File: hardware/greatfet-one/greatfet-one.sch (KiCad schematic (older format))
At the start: 99 parts, among them J1 NEIGHBOR1, J2 NEIGHBOR2, J3 USB-MICRO-B-SHIELDED, J4 USB-MICRO-B-SHIELDED, J5 JTAG, J6 POWER, J7 BONUS_ROW, SW1 DFU, SW2 RESET, U1 LPC4330FBD144, U2 W25Q16DV, U3 AP7333, U4 IP4220CZ6, U5 AP2553W6-7, X1 MCU_XTAL, X2 RTC_XTAL

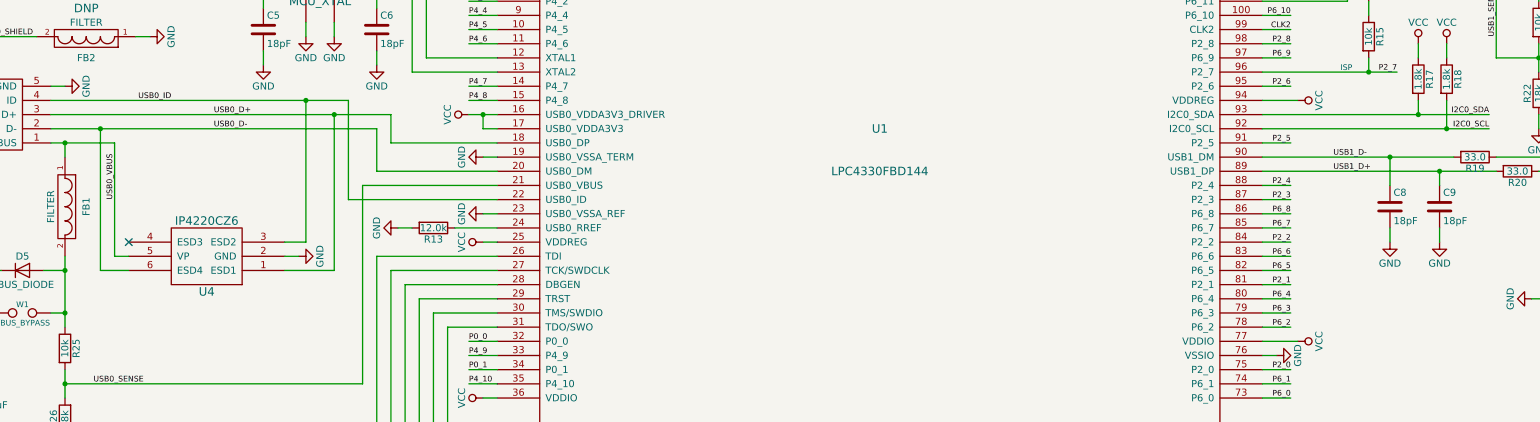
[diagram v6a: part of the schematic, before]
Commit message: GreatFET One: added 15k pull-down resistors to USB signals to support host mode
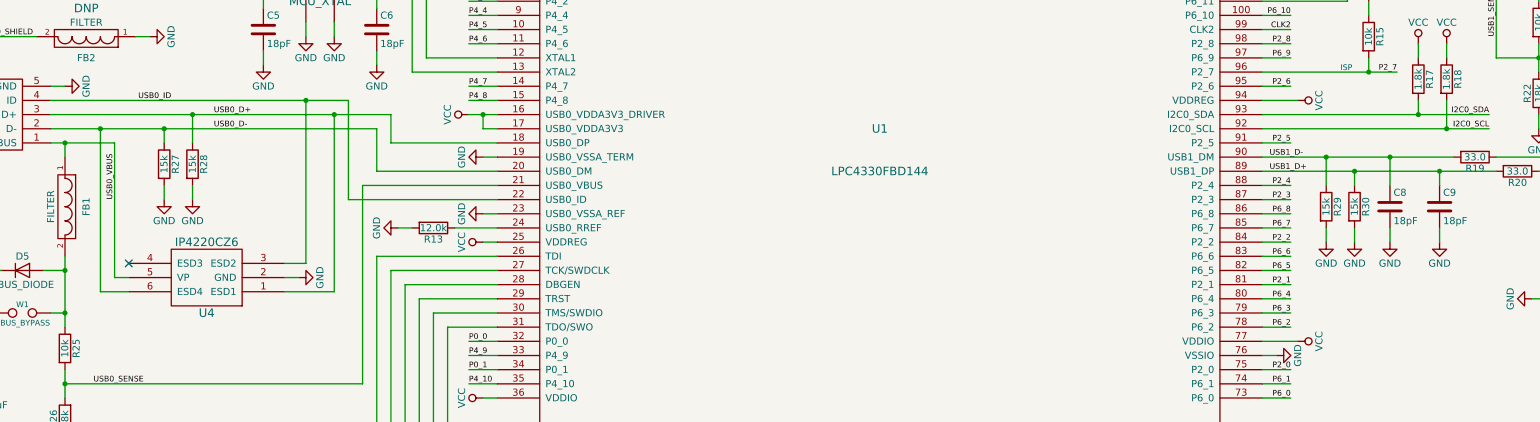
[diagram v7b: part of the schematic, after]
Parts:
- added R27, R28, R29, R30: 15k, gsg-modules:0603, symbol R
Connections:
- net GND: now also R27.2, R28.2, R29.2, R30.2
- net USB0_D+: now also R28.1
- net USB0_D-: now also R27.1
- net USB1_D+: now also R30.1
- net USB1_D-: now also R29.1
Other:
- moved on the sheet: U4
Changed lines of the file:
@@
 EESchema Schematic File Version 2
-LIBS:greatfet-one-rescue
 LIBS:power
 LIBS:device
@@
 LIBS:contrib
 LIBS:valves
-LIBS:gsg-symbols
 LIBS:greatfet-one-cache
 EELAYER 25 0
@@
 L IP4220CZ6 U4
 U 1 1 55E0B467
-P 3800 6100
-F 0 "U4" H 3800 6350 60  0000 C CNN
-F 1 "IP4220CZ6" H 3800 5850 60  0000 C CNN
-F 2 "gsg-modules:SOT457" H 3800 6100 60  0001 C CNN
-F 3 "" H 3800 6100 60  0000 C CNN
-F 4 "NXP" H 3800 6100 60  0001 C CNN "Manufacturer"
-F 5 "IP4220CZ6,125" H 3800 6100 60  0001 C CNN "Part Number"
-F 6 "IC USB DUAL ESD PROTECT 6TSOP" H 3800 6100 60  0001 C CNN "Description"
-	1    3800 6100
+P 3800 6250
+F 0 "U4" H 3800 6500 60  0000 C CNN
+F 1 "IP4220CZ6" H 3800 6000 60  0000 C CNN
+F 2 "gsg-modules:SOT457" H 3800 6250 60  0001 C CNN
+F 3 "" H 3800 6250 60  0000 C CNN
+F 4 "NXP" H 3800 6250 60  0001 C CNN "Manufacturer"
+F 5 "IP4220CZ6,125" H 3800 6250 60  0001 C CNN "Part Number"
+F 6 "IC USB DUAL ESD PROTECT 6TSOP" H 3800 6250 60  0001 C CNN "Description"
+	1    3800 6250
 	-1   0    0    1
 $EndComp
@@
 L GND #PWR011
 U 1 1 55E3AB7C
-P 4450 6100
-F 0 "#PWR011" H 4450 5850 50  0001 C CNN
-F 1 "GND" H 4450 5950 50  0000 C CNN
-F 2 "" H 4450 6100 60  0000 C CNN
-F 3 "" H 4450 6100 60  0000 C CNN
-	1    4450 6100
+P 4450 6250
+F 0 "#PWR011" H 4450 6000 50  0001 C CNN
+F 1 "GND" H 4450 6100 50  0000 C CNN
+F 2 "" H 4450 6250 60  0000 C CNN
+F 3 "" H 4450 6250 60  0000 C CNN
+	1    4450 6250
 	0    -1   -1   0
 $EndComp
@@
 Text Label 3850 5200 0    40   ~ 0
 USB0_D-
-Text Label 11750 5400 0    40   ~ 0
+Text Label 11300 5400 0    40   ~ 0
 USB1_D-
-Text Label 11750 5500 0    40   ~ 0
+Text Label 11300 5500 0    40   ~ 0
 USB1_D+
-NoConn ~ 3250 6000
+NoConn ~ 3250 6150
 Text Label 2200 4550 0    40   ~ 0
 USB0_SHIELD
@@
 	0    1    1    0
 $EndComp
+$Comp
+L VCC #PWR092
+U 1 1 57C6226E
+P 5900 1400
+F 0 "#PWR092" H 5900 1250 50  0001 C CNN
+F 1 "VCC" H 5900 1550 50  0000 C CNN
+F 2 "" H 5900 1400 60  0000 C CNN
+F 3 "" H 5900 1400 60  0000 C CNN
+	1    5900 1400
+	0    -1   -1   0
+$EndComp
+Text Label 5750 1200 0    40   ~ 0
+USB1_VBUS
+$Comp
+L TEST_2P W1
+U 1 1 57C655EF
+P 2500 6500
+F 0 "W1" H 2500 6560 40  0000 C CNN
+F 1 "VBUS_BYPASS" H 2500 6430 40  0000 C CNN
+F 2 "gsg-modules:0603-JUMPER" H 2500 6500 60  0001 C CNN
+F 3 "" H 2500 6500 60  0000 C CNN
+	1    2500 6500
+	1    0    0    -1
+$EndComp
+$Comp
+L R R28
+U 1 1 5A48D952
+P 3700 5450
+F 0 "R28" V 3780 5450 50  0000 C CNN
+F 1 "15k" V 3700 5450 50  0000 C CNN
+F 2 "gsg-modules:0603" V 3630 5450 30  0001 C CNN
+F 3 "" H 3700 5450 30  0000 C CNN
+F 4 "Yageo" H 3700 5450 60  0001 C CNN "Manufacturer"
+F 5 "RC0603JR-0715KL" H 3700 5450 60  0001 C CNN "Part Number"
+F 6 "RES SMD 15K OHM 5% 1/10W 0603" H 3700 5450 60  0001 C CNN "Description"
+	1    3700 5450
+	1    0    0    -1
+$EndComp
+$Comp
+L R R27
+U 1 1 5A48E55C
+P 3500 5450
+F 0 "R27" V 3580 5450 50  0000 C CNN
+F 1 "15k" V 3500 5450 50  0000 C CNN
+F 2 "gsg-modules:0603" V 3430 5450 30  0001 C CNN
+F 3 "" H 3500 5450 30  0000 C CNN
+F 4 "Yageo" H 3500 5450 60  0001 C CNN "Manufacturer"
+F 5 "RC0603JR-0715KL" H 3500 5450 60  0001 C CNN "Part Number"
+F 6 "RES SMD 15K OHM 5% 1/10W 0603" H 3500 5450 60  0001 C CNN "Description"
+	1    3500 5450
+	1    0    0    -1
+$EndComp
+$Comp
+L GND #PWR093
+U 1 1 5A48EE95
+P 3500 5700
+F 0 "#PWR093" H 3500 5450 50  0001 C CNN
+F 1 "GND" H 3500 5550 50  0000 C CNN
+F 2 "" H 3500 5700 60  0000 C CNN
+F 3 "" H 3500 5700 60  0000 C CNN
+	1    3500 5700
+	1    0    0    -1
+$EndComp
+$Comp
+L GND #PWR094
+U 1 1 5A48EFCF
+P 3700 5700
+F 0 "#PWR094" H 3700 5450 50  0001 C CNN
+F 1 "GND" H 3700 5550 50  0000 C CNN
+F 2 "" H 3700 5700 60  0000 C CNN
+F 3 "" H 3700 5700 60  0000 C CNN
+	1    3700 5700
+	1    0    0    -1
+$EndComp
+$Comp
+L R R30
+U 1 1 5A4907DE
+P 11900 5750
+F 0 "R30" V 11980 5750 50  0000 C CNN
+F 1 "15k" V 11900 5750 50  0000 C CNN
+F 2 "gsg-modules:0603" V 11830 5750 30  0001 C CNN
+F 3 "" H 11900 5750 30  0000 C CNN
+F 4 "Yageo" H 11900 5750 60  0001 C CNN "Manufacturer"
+F 5 "RC0603JR-0715KL" H 11900 5750 60  0001 C CNN "Part Number"
+F 6 "RES SMD 15K OHM 5% 1/10W 0603" H 11900 5750 60  0001 C CNN "Description"
+	1    11900 5750
+	1    0    0    -1
+$EndComp
+$Comp
+L R R29
+U 1 1 5A4907E7
+P 11700 5750
+F 0 "R29" V 11780 5750 50  0000 C CNN
+F 1 "15k" V 11700 5750 50  0000 C CNN
+F 2 "gsg-modules:0603" V 11630 5750 30  0001 C CNN
+F 3 "" H 11700 5750 30  0000 C CNN
+F 4 "Yageo" H 11700 5750 60  0001 C CNN "Manufacturer"
+F 5 "RC0603JR-0715KL" H 11700 5750 60  0001 C CNN "Part Number"
+F 6 "RES SMD 15K OHM 5% 1/10W 0603" H 11700 5750 60  0001 C CNN "Description"
+	1    11700 5750
+	1    0    0    -1
+$EndComp
+$Comp
+L GND #PWR095
+U 1 1 5A4907ED
+P 11700 6000
+F 0 "#PWR095" H 11700 5750 50  0001 C CNN
+F 1 "GND" H 11700 5850 50  0000 C CNN
+F 2 "" H 11700 6000 60  0000 C CNN
+F 3 "" H 11700 6000 60  0000 C CNN
+	1    11700 6000
+	1    0    0    -1
+$EndComp
+$Comp
+L GND #PWR096
+U 1 1 5A4907F3
+P 11900 6000
+F 0 "#PWR096" H 11900 5750 50  0001 C CNN
+F 1 "GND" H 11900 5850 50  0000 C CNN
+F 2 "" H 11900 6000 60  0000 C CNN
+F 3 "" H 11900 6000 60  0000 C CNN
+	1    11900 6000
+	1    0    0    -1
+$EndComp
 Wire Wire Line
 	7500 8250 7500 8050
@@
 Connection ~ 12150 5400
 Wire Wire Line
-	12500 5600 12500 5500
+	12500 5500 12500 5600
 Connection ~ 12500 5500
 Wire Wire Line
@@
 	13550 5700 13450 5700
 Wire Wire Line
-	4350 6000 4500 6000
+	4350 6150 4500 6150
 Wire Wire Line
-	4350 6200 4700 6200
+	4350 6350 4700 6350
 Wire Wire Line
-	4350 6100 4450 6100
+	4350 6250 4450 6250
 Wire Wire Line
-	3250 6100 3150 6100
+	3250 6250 3150 6250
 Wire Wire Line
-	3150 6100 3150 5300
+	3150 6250 3150 5300
 Wire Wire Line
 	1850 6700 1950 6700
@@
 Connection ~ 3050 5200
 Wire Wire Line
-	4700 6200 4700 5100
+	4700 6350 4700 5100
 Connection ~ 4700 5100
 Wire Wire Line
-	4500 6000 4500 5000
+	4500 6150 4500 5000
 Connection ~ 4500 5000
 Wire Wire Line
-	3250 6200 3050 6200
+	3250 6350 3050 6350
 Wire Wire Line
-	3050 6200 3050 5200
+	3050 6350 3050 5200
 Wire Wire Line
 	2800 7400 2800 7500
@@
 Wire Wire Line
 	6000 1300 6100 1300
-$Comp
-L VCC #PWR092
-U 1 1 57C6226E
-P 5900 1400
-F 0 "#PWR092" H 5900 1250 50  0001 C CNN
-F 1 "VCC" H 5900 1550 50  0000 C CNN
-F 2 "" H 5900 1400 60  0000 C CNN
-F 3 "" H 5900 1400 60  0000 C CNN
-	1    5900 1400
-	0    -1   -1   0
-$EndComp
 Wire Wire Line
 	5900 1400 6100 1400
-Text Label 5750 1200 0    40   ~ 0
-USB1_VBUS
 Wire Wire Line
 	5750 1200 6100 1200
-$Comp
-L TEST_2P W1
-U 1 1 57C655EF
-P 2500 6500
-F 0 "W1" H 2500 6560 40  0000 C CNN
-F 1 "VBUS_BYPASS" H 2500 6430 40  0000 C CNN
-F 2 "gsg-modules:0603-JUMPER" H 2500 6500 60  0001 C CNN
-F 3 "" H 2500 6500 60  0000 C CNN
-	1    2500 6500
-	1    0    0    -1
-$EndComp
 Wire Wire Line
 	2200 6500 2300 6500
@@
 	2700 6500 2800 6500
 Connection ~ 2800 6500
+Wire Wire Line
+	3700 5100 3700 5300
+Connection ~ 3700 5100
+Wire Wire Line
+	3500 5700 3500 5600
+Wire Wire Line
+	3700 5700 3700 5600
+Wire Wire Line
+	11700 6000 11700 5900
+Wire Wire Line
+	11900 6000 11900 5900
+Wire Wire Line
+	11700 5400 11700 5600
+Connection ~ 11700 5400
+Wire Wire Line
+	11900 5500 11900 5600
+Connection ~ 11900 5500
+Wire Wire Line
+	3500 5300 3500 5200
+Connection ~ 3500 5200
 $EndSCHEMATC

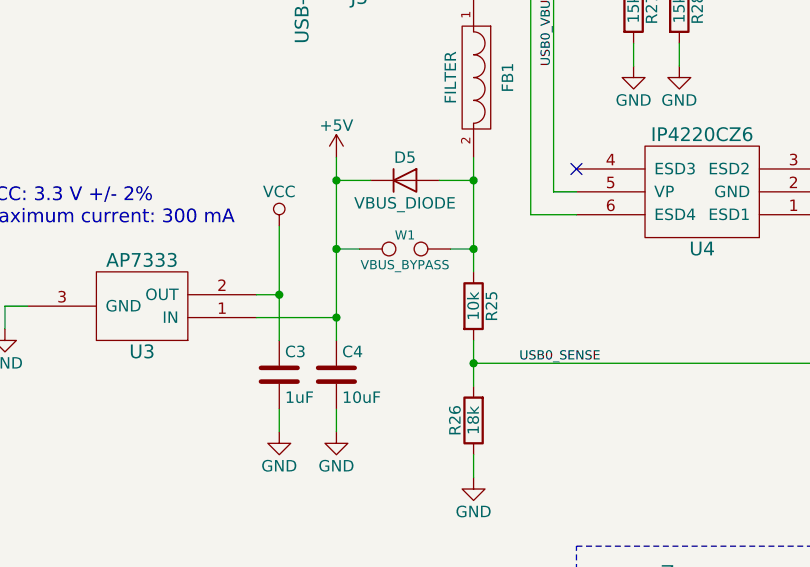
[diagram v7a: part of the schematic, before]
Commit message: GreatFET One: marked W1 test point DNP
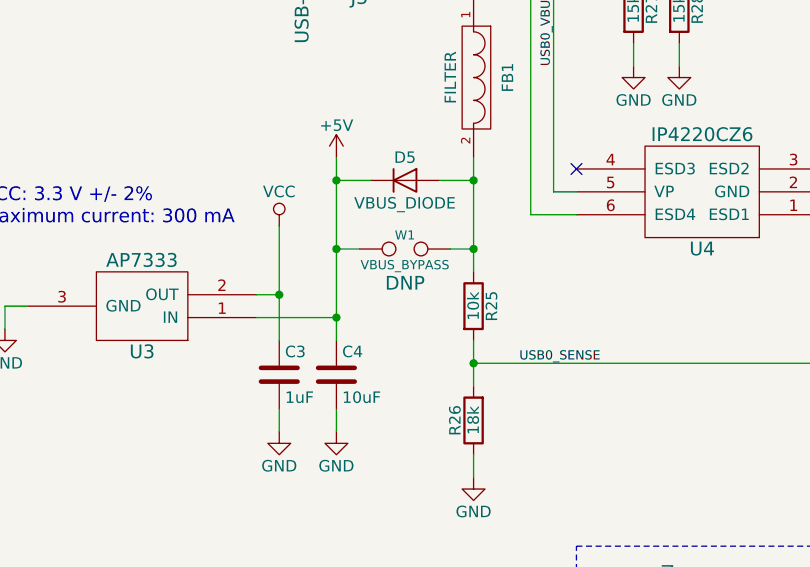
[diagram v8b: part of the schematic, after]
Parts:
- W1: Note (none) -> DNP
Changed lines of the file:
@@
 LIBS:contrib
 LIBS:valves
+LIBS:gsg-symbols
 LIBS:greatfet-one-cache
 EELAYER 25 0
@@
 F 2 "gsg-modules:0603-JUMPER" H 2500 6500 60  0001 C CNN
 F 3 "" H 2500 6500 60  0000 C CNN
+F 4 "DNP" H 2500 6350 60  0000 C CNN "Note"
 	1    2500 6500
 	1    0    0    -1
